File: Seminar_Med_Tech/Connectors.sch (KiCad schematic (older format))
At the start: 21 parts

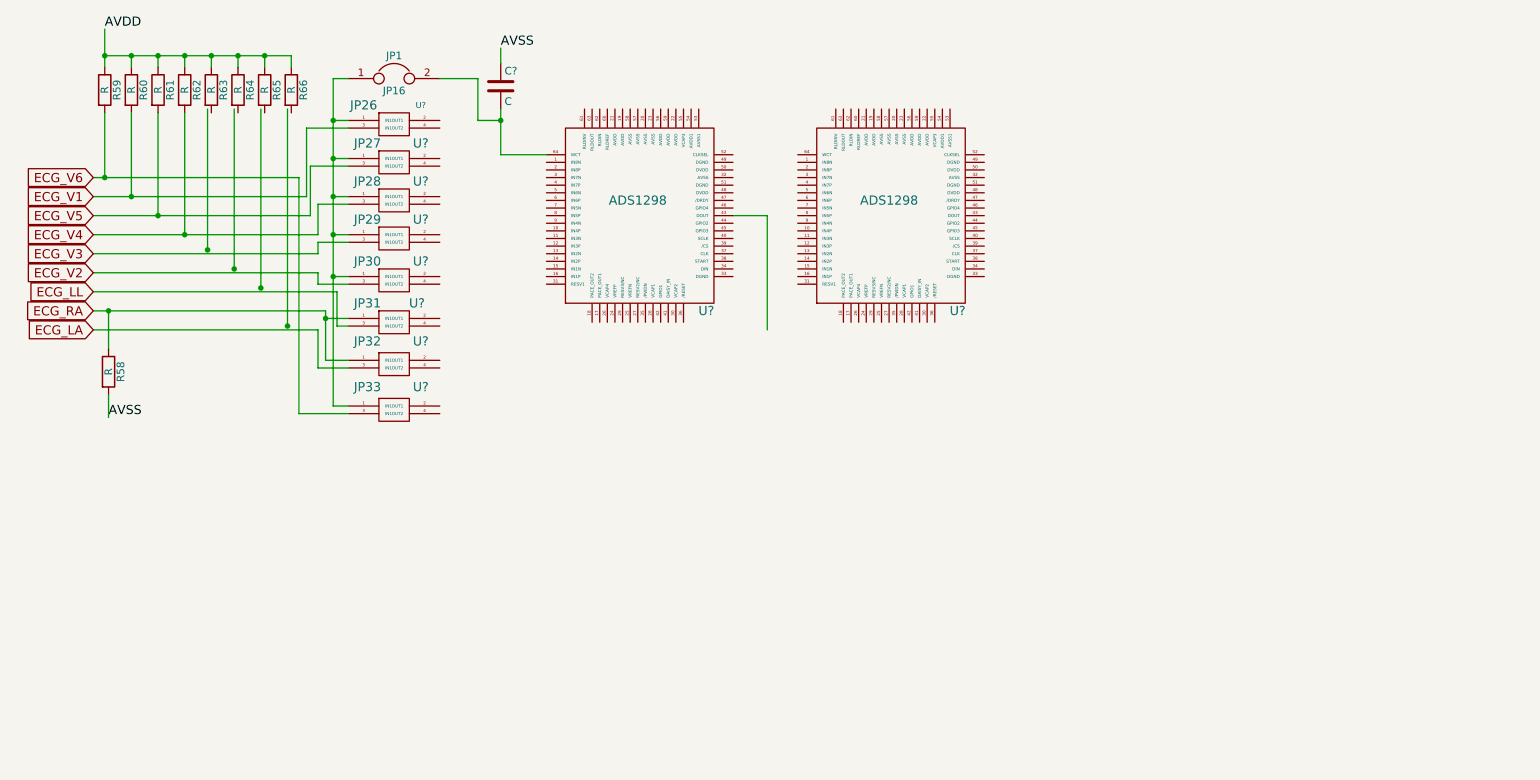
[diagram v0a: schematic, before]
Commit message: Updated Dokumentation and connectors
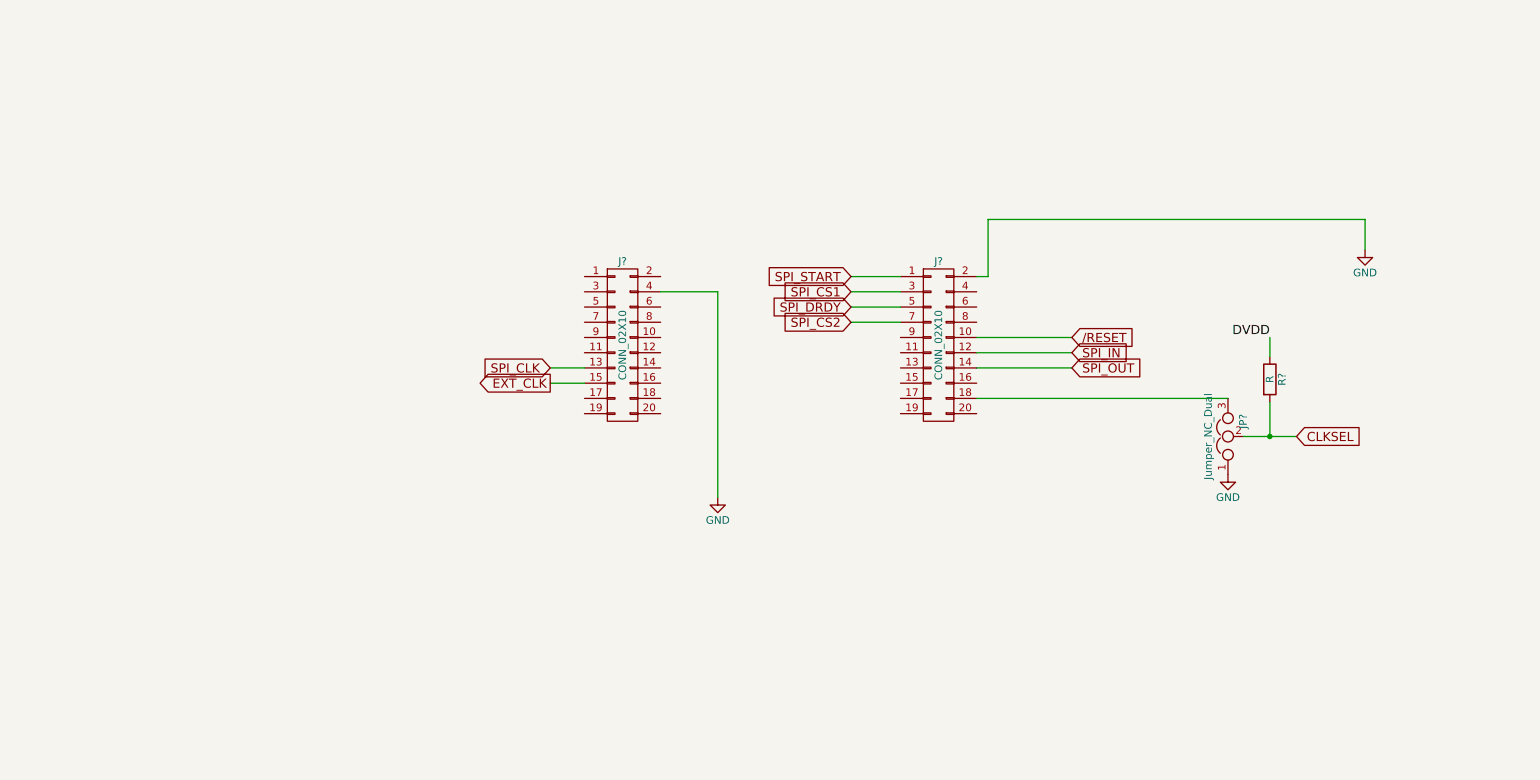
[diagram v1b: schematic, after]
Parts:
- removed C?: C, symbol C
- removed JP1: JP16, symbol Jumper
- removed R58, R59, R60, R61, R62, R63, R64, R65, R66: R, symbol R
- removed U?: JP26, symbol Jumper2x2
- removed U?: JP27, symbol Jumper2x2
- removed U?: JP28, symbol Jumper2x2
- removed U?: JP29, symbol Jumper2x2
- removed U?: JP30, symbol Jumper2x2
- removed U?: JP31, symbol Jumper2x2
- removed U?: JP32, symbol Jumper2x2
- removed U?: JP33, symbol Jumper2x2
- removed U? (x2): ADS1298, symbol ADS1298
- added J? (x2): CONN_02X10, symbol CONN_02X10
- added JP?: Jumper_NC_Dual, symbol Jumper_NC_Dual
- added R?: R, symbol R
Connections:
- net labels added: /RESET, CLKSEL, DVDD, EXT_CLK, GND, SPI_CLK, SPI_CS1, SPI_CS2, SPI_DRDY, SPI_IN, SPI_OUT, SPI_START
- net labels removed: AVDD, AVSS, ECG_LA, ECG_LL, ECG_RA, ECG_V1, ECG_V2, ECG_V3, ECG_V4, ECG_V5, ECG_V6
- wire segments 63 -> 19

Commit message: Updated connectors
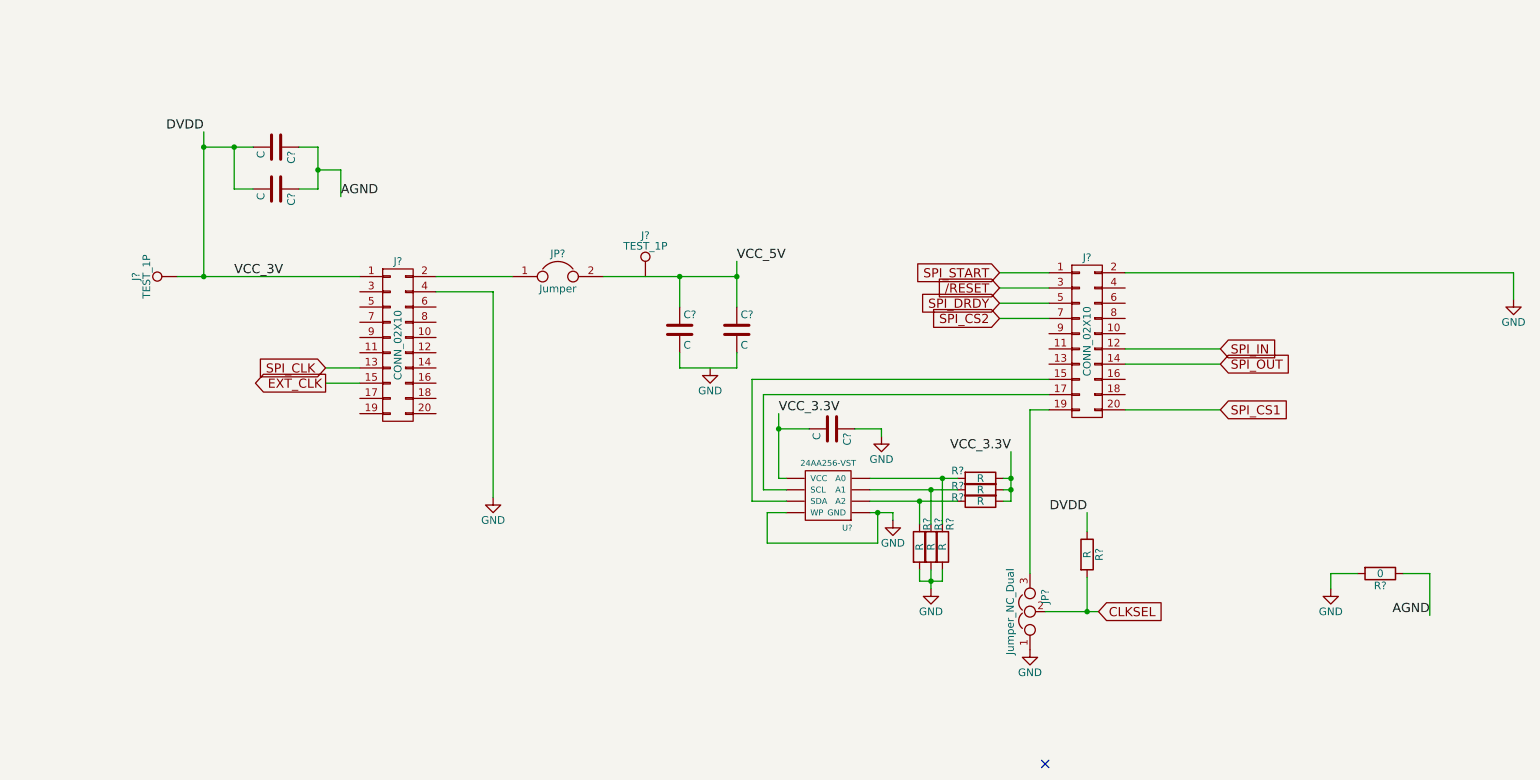
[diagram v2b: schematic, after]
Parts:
- added C? (x5): C, symbol C
- added J? (x2): TEST_1P, symbol TEST_1P
- added JP?: Jumper, symbol Jumper
- added R?: 0, symbol R
- added R? (x6): R, symbol R
- added U?: 24AA256-VST, symbol 24AA256-VST
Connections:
- net /RESET: now also J?.3 (P3); no longer J?.10 (P10)
- net DVDD: now also J?.1 (P1), C?.2, C?.2, J?.1
- net GND: now also C?.1, R?.2, R?.2, R?.2, R?.2, U?.~ (WP)
- net SPI_CS1: now also J?.20 (P20); no longer J?.3 (P3)
- net at J?.2 (P2): now also JP?.1
- net at J?.15 (P15): now also U?.~ (WP)
- net at J?.17 (P17): now also U?.~ (WP)
- net at J?.18 (P18): no longer JP?.3
- net at J?.19 (P19): now also JP?.3
- new net: C?.2, C?.2
- new net: R?.1, R?.2, U?.~ (WP) (x3)
- new net AGND: C?.1, C?.1, R?.1
- new net VCC_3.3V: C?.2, R?.1, R?.1, R?.1, U?.~ (WP)
- new net VCC_5V: C?.1, C?.1, JP?.2
- no-connect marks 0 -> 1
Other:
- moved on the sheet: J?, JP?, R?

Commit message: Updated connectors
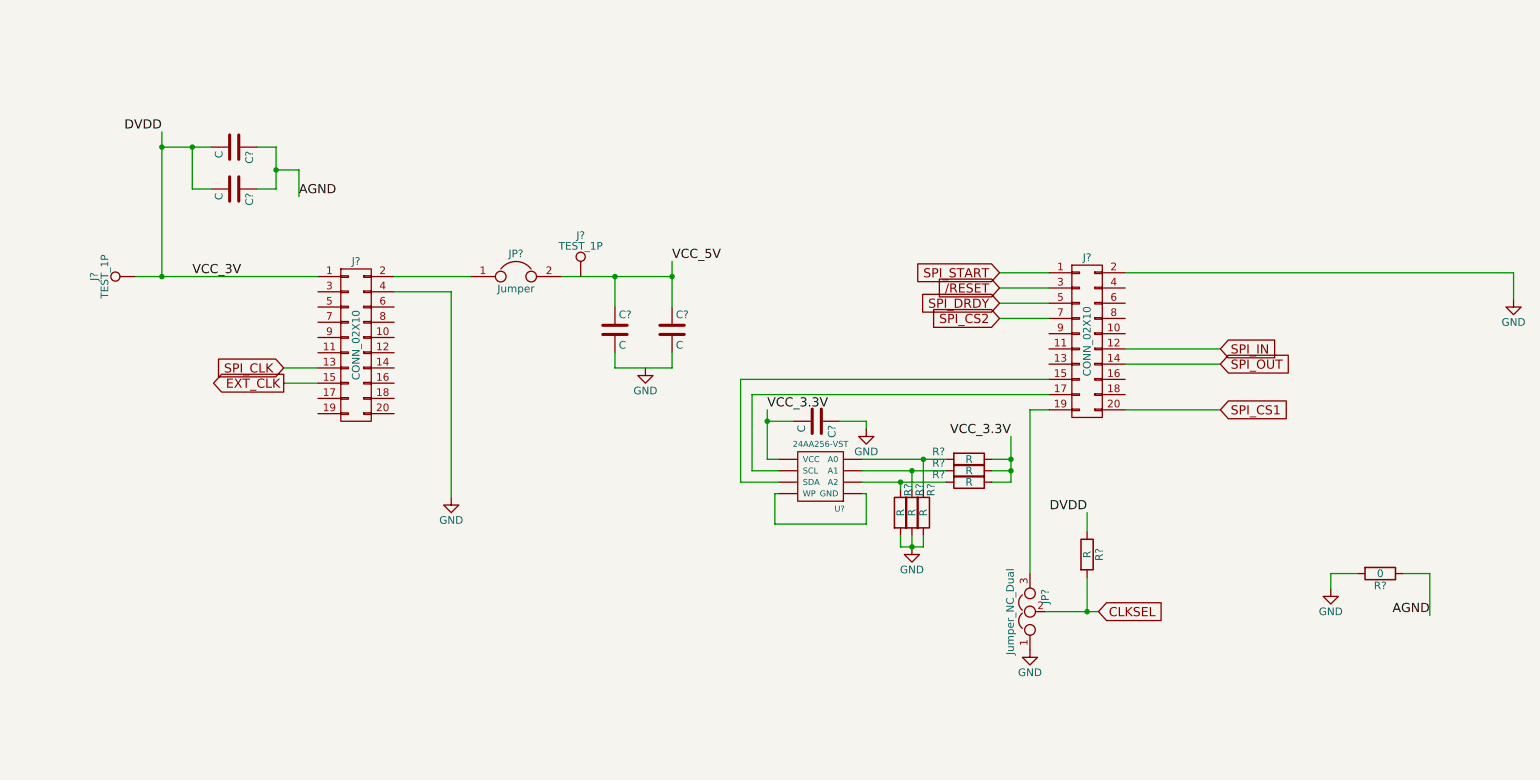
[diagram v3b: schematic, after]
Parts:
- removed C?: C, symbol C
- removed R? (x6): R, symbol R
- removed U?: 24AA256-VST, symbol 24AA256-VST
- added C?: C, symbol C
- added R? (x6): R, symbol R
- added U?: 24AA256-VST, symbol 24AA256-VST
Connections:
- net GND: now also C?.1, R?.2, R?.2, R?.2
- net VCC_3.3V: now also C?.2, R?.1, R?.1, R?.1, U?.~ (WP)
- net at J?.15 (P15): now also U?.~ (WP)
- net at J?.17 (P17): now also U?.~ (WP)
- new net: R?.1, R?.2, U?.~ (WP) (x3)
- no-connect marks 1 -> 0
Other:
- moved on the sheet: C?, J?, JP?

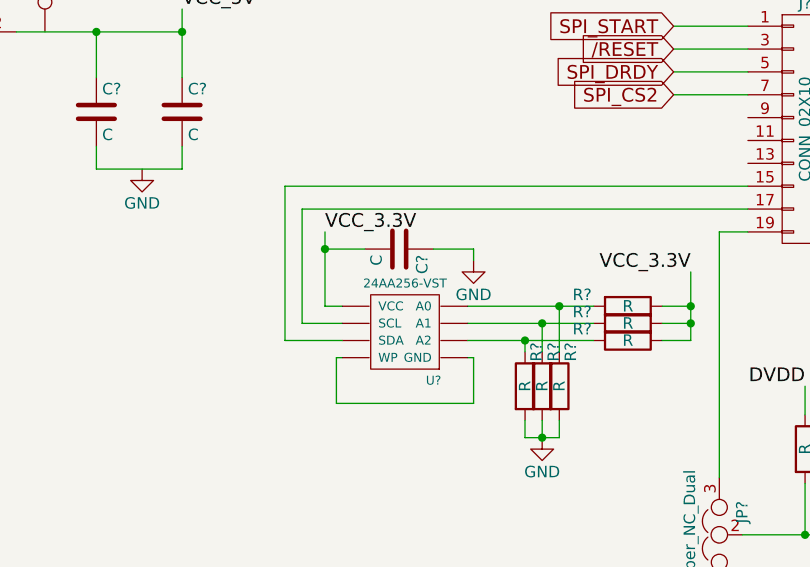
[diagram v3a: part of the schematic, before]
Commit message: Updated connectors
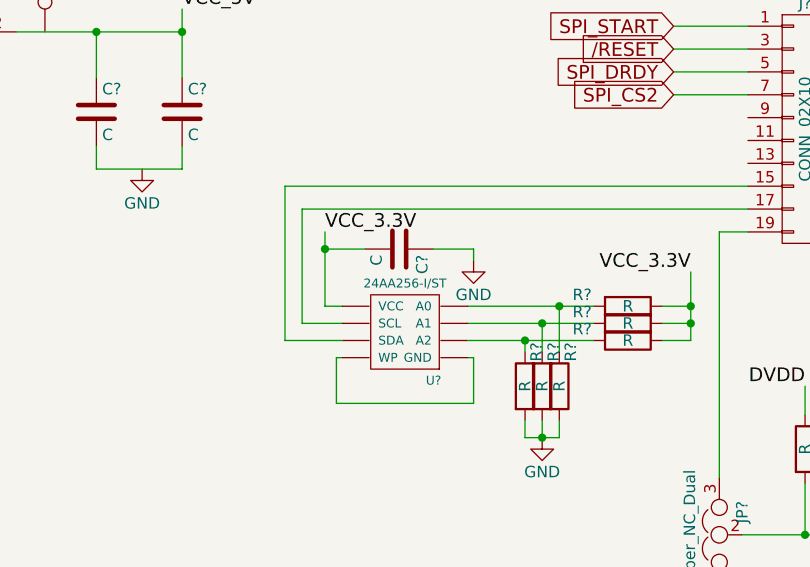
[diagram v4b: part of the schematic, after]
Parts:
- removed U?: 24AA256-VST, symbol 24AA256-VST
- added U?: 24AA256-I/ST, symbol 24AA256-I/ST
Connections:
- net VCC_3.3V: now also U?.~ (WP)
- net at J?.15 (P15): now also U?.~ (WP)
- net at J?.17 (P17): now also U?.~ (WP)
- net at R?.1, R?.2: now also U?.~ (WP) (x3)
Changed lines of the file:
@@
 VCC_5V
-$Comp
-L 24AA256-VST U?
-U 1 1 593E8EFE
-P 5850 4875
-F 0 "U?" H 5975 4675 39  0000 C CNN
-F 1 "24AA256-VST" H 5850 5100 39  0000 C CNN
-F 2 "" H 5850 4875 60  0001 C CNN
-F 3 "" H 5850 4875 60  0001 C CNN
-	1    5850 4875
-	1    0    0    -1
-$EndComp
 $Comp
 L C C?
@@
 Text Label 5500 4425 0    60   ~ 0
 VCC_3.3V
+$Comp
+L 24AA256-I/ST U?
+U 1 1 593E975F
+P 5850 4875
+F 0 "U?" H 5975 4675 39  0000 C CNN
+F 1 "24AA256-I/ST" H 5850 5100 39  0000 C CNN
+F 2 "" H 5850 4875 60  0001 C CNN
+F 3 "" H 5850 4875 60  0001 C CNN
+	1    5850 4875
+	1    0    0    -1
+$EndComp
 $EndSCHEMATC

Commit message: Updated
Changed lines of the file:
@@
 L GND #PWR?
 U 1 1 593AE149
-P 10400 3700
-F 0 "#PWR?" H 10400 3450 50  0001 C CNN
-F 1 "GND" H 10400 3550 50  0000 C CNN
-F 2 "" H 10400 3700 50  0001 C CNN
-F 3 "" H 10400 3700 50  0001 C CNN
-	1    10400 3700
+P 8900 3700
+F 0 "#PWR?" H 8900 3450 50  0001 C CNN
+F 1 "GND" H 8900 3550 50  0000 C CNN
+F 2 "" H 8900 3700 50  0001 C CNN
+F 3 "" H 8900 3700 50  0001 C CNN
+	1    8900 3700
 	1    0    0    -1
 $EndComp
@@
 	3425 3650 3425 5000
 Wire Wire Line
-	7850 3525 10400 3525
-Wire Wire Line
-	10400 3525 10400 3700
+	7850 3525 8900 3525
+Wire Wire Line
+	8900 3525 8900 3700
 Wire Wire Line
 	7850 4425 8475 4425

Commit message: Update
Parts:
- removed C?: C, symbol C
- removed R? (x6): R, symbol R
- removed U?: 24AA256-I/ST, symbol 24AA256-I/ST
- JP21: renamed from JP?; value Jumper_NC_Dual -> Jumper
- gave numbers to parts that had none: 1
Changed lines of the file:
@@
 EXT_CLK
 $Comp
-L Jumper_NC_Dual JP?
+L Jumper_NC_Dual JP21
 U 1 1 593ADF16
 P 7225 5750
-F 0 "JP?" H 7275 5650 50  0000 L CNN
-F 1 "Jumper_NC_Dual" H 7225 5850 50  0000 C BNN
+F 0 "JP21" H 7275 5650 50  0000 L CNN
+F 1 "Jumper" H 7225 5850 50  0000 C BNN
 F 2 "" H 7225 5750 50  0001 C CNN
 F 3 "" H 7225 5750 50  0001 C CNN
@@
 AGND
 $Comp
-L Jumper JP?
+L Jumper JP3
 U 1 1 593E89D7
 P 3850 3550
-F 0 "JP?" H 3850 3700 50  0000 C CNN
+F 0 "JP3" H 3850 3700 50  0000 C CNN
 F 1 "Jumper" H 3850 3470 50  0000 C CNN
 F 2 "" H 3850 3550 50  0001 C CNN
@@
 Text Label 4875 3450 0    60   ~ 0
 VCC_5V
-$Comp
-L C C?
-U 1 1 593E9129
-P 5825 4500
-F 0 "C?" H 5850 4600 50  0000 L CNN
-F 1 "C" H 5850 4400 50  0000 L CNN
-F 2 "" H 5863 4350 50  0001 C CNN
-F 3 "" H 5825 4500 50  0001 C CNN
-	1    5825 4500
-	0    1    1    0
-$EndComp
-$Comp
-L GND #PWR?
-U 1 1 593E9213
-P 6150 4550
-F 0 "#PWR?" H 6150 4300 50  0001 C CNN
-F 1 "GND" H 6150 4400 50  0000 C CNN
-F 2 "" H 6150 4550 50  0001 C CNN
-F 3 "" H 6150 4550 50  0001 C CNN
-	1    6150 4550
-	1    0    0    -1
-$EndComp
-$Comp
-L R R?
-U 1 1 593E92E1
-P 6825 4750
-F 0 "R?" V 6775 4550 50  0000 C CNN
-F 1 "R" V 6825 4750 50  0000 C CNN
-F 2 "" V 6755 4750 50  0001 C CNN
-F 3 "" H 6825 4750 50  0001 C CNN
-	1    6825 4750
-	0    1    1    0
-$EndComp
-$Comp
-L R R?
-U 1 1 593E9373
-P 6825 4825
-F 0 "R?" V 6775 4625 50  0000 C CNN
-F 1 "R" V 6825 4825 50  0000 C CNN
-F 2 "" V 6755 4825 50  0001 C CNN
-F 3 "" H 6825 4825 50  0001 C CNN
-	1    6825 4825
-	0    1    1    0
-$EndComp
-$Comp
-L R R?
-U 1 1 593E946E
-P 6825 4900
-F 0 "R?" V 6775 4700 50  0000 C CNN
-F 1 "R" V 6825 4900 50  0000 C CNN
-F 2 "" V 6755 4900 50  0001 C CNN
-F 3 "" H 6825 4900 50  0001 C CNN
-	1    6825 4900
-	0    1    1    0
-$EndComp
-Text Label 7100 4600 2    60   ~ 0
-VCC_3.3V
-$Comp
-L R R?
-U 1 1 593E9A02
-P 6525 5100
-F 0 "R?" V 6575 5250 50  0000 C CNN
-F 1 "R" V 6525 5100 50  0000 C CNN
-F 2 "" V 6455 5100 50  0001 C CNN
-F 3 "" H 6525 5100 50  0001 C CNN
-	1    6525 5100
-	1    0    0    -1
-$EndComp
-$Comp
-L R R?
-U 1 1 593E9A4D
-P 6450 5100
-F 0 "R?" V 6500 5250 50  0000 C CNN
-F 1 "R" V 6450 5100 50  0000 C CNN
-F 2 "" V 6380 5100 50  0001 C CNN
-F 3 "" H 6450 5100 50  0001 C CNN
-	1    6450 5100
-	1    0    0    -1
-$EndComp
-$Comp
-L R R?
-U 1 1 593E9A8E
-P 6375 5100
-F 0 "R?" V 6425 5250 50  0000 C CNN
-F 1 "R" V 6375 5100 50  0000 C CNN
-F 2 "" V 6305 5100 50  0001 C CNN
-F 3 "" H 6375 5100 50  0001 C CNN
-	1    6375 5100
-	1    0    0    -1
-$EndComp
 Wire Wire Line
 	2550 4150 2325 4150
@@
 	4875 4150 4875 4050
 Connection ~ 4875 3550
-Wire Wire Line
-	5575 4825 5400 4825
-Wire Wire Line
-	5400 4825 5400 4325
-Wire Wire Line
-	5400 4325 7350 4325
-Wire Wire Line
-	7350 4225 5325 4225
-Wire Wire Line
-	5325 4225 5325 4900
-Wire Wire Line
-	5325 4900 5575 4900
-Wire Wire Line
-	6125 4975 6150 4975
-Wire Wire Line
-	6150 4975 6150 5175
-Wire Wire Line
-	6150 5175 5550 5175
-Wire Wire Line
-	5550 5175 5550 4975
-Wire Wire Line
-	5550 4975 5575 4975
-Wire Wire Line
-	5500 4425 5500 4500
-Wire Wire Line
-	5500 4500 5500 4750
-Wire Wire Line
-	5500 4750 5575 4750
-Wire Wire Line
-	5675 4500 5500 4500
-Connection ~ 5500 4500
-Wire Wire Line
-	5975 4500 6150 4500
-Wire Wire Line
-	6150 4500 6150 4550
-Wire Wire Line
-	6675 4750 6525 4750
-Wire Wire Line
-	6525 4750 6125 4750
-Wire Wire Line
-	6125 4825 6450 4825
-Wire Wire Line
-	6450 4825 6675 4825
-Wire Wire Line
-	6675 4900 6375 4900
-Wire Wire Line
-	6375 4900 6125 4900
-Wire Wire Line
-	6975 4750 7100 4750
-Wire Wire Line
-	7100 4825 6975 4825
-Wire Wire Line
-	7100 4900 6975 4900
-Wire Wire Line
-	7100 4600 7100 4750
-Wire Wire Line
-	7100 4750 7100 4825
-Wire Wire Line
-	7100 4825 7100 4900
-Connection ~ 7100 4825
-Connection ~ 7100 4750
-Wire Wire Line
-	6525 4750 6525 4950
-Connection ~ 6525 4750
-Wire Wire Line
-	6450 4950 6450 4825
-Connection ~ 6450 4825
-Wire Wire Line
-	6375 4900 6375 4950
-Connection ~ 6375 4900
-Wire Wire Line
-	6375 5250 6375 5325
-Wire Wire Line
-	6375 5325 6450 5325
-Wire Wire Line
-	6450 5325 6525 5325
-Wire Wire Line
-	6525 5325 6525 5250
-Wire Wire Line
-	6450 5250 6450 5325
-Connection ~ 6450 5325
-$Comp
-L GND #PWR?
-U 1 1 593E9DBC
-P 6450 5325
-F 0 "#PWR?" H 6450 5075 50  0001 C CNN
-F 1 "GND" H 6450 5175 50  0000 C CNN
-F 2 "" H 6450 5325 50  0001 C CNN
-F 3 "" H 6450 5325 50  0001 C CNN
-	1    6450 5325
-	1    0    0    -1
-$EndComp
-Text Label 5500 4425 0    60   ~ 0
-VCC_3.3V
-$Comp
-L 24AA256-I/ST U?
-U 1 1 593E975F
-P 5850 4875
-F 0 "U?" H 5975 4675 39  0000 C CNN
-F 1 "24AA256-I/ST" H 5850 5100 39  0000 C CNN
-F 2 "" H 5850 4875 60  0001 C CNN
-F 3 "" H 5850 4875 60  0001 C CNN
-	1    5850 4875
-	1    0    0    -1
-$EndComp
 $EndSCHEMATC

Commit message: Update
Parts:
- C68, C71: renamed from C?; value C -> 100uF
- C69, C70: renamed from C?; value C -> 0.1uF
- J?: value TEST_1P -> TP10
- J?: value TEST_1P -> TP7
- R67: renamed from R?; value R -> 10K
- gave numbers to parts that had none: 1
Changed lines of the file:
@@
 CLKSEL
 $Comp
-L R R?
+L R R67
 U 1 1 593ADFF6
 P 7600 5375
-F 0 "R?" V 7680 5375 50  0000 C CNN
-F 1 "R" V 7600 5375 50  0000 C CNN
+F 0 "R67" V 7680 5375 50  0000 C CNN
+F 1 "10K" V 7600 5375 50  0000 C CNN
 F 2 "" V 7530 5375 50  0001 C CNN
 F 3 "" H 7600 5375 50  0001 C CNN
@@
 $EndComp
 $Comp
-L R R?
+L R R74
 U 1 1 593E72CF
 P 9525 5500
-F 0 "R?" V 9605 5500 50  0000 C CNN
+F 0 "R74" V 9605 5500 50  0000 C CNN
 F 1 "0" V 9525 5500 50  0000 C CNN
 F 2 "" V 9455 5500 50  0001 C CNN
@@
 P 1350 3550
 F 0 "J?" H 1350 3820 50  0000 C CNN
-F 1 "TEST_1P" H 1350 3750 50  0000 C CNN
+F 1 "TP10" H 1350 3750 50  0000 C CNN
 F 2 "" H 1550 3550 50  0001 C CNN
 F 3 "" H 1550 3550 50  0001 C CNN
@@
 DVDD
 $Comp
-L C C?
+L C C71
 U 1 1 593E8011
 P 2000 2700
-F 0 "C?" H 2025 2800 50  0000 L CNN
-F 1 "C" H 2025 2600 50  0000 L CNN
+F 0 "C71" H 2025 2800 50  0000 L CNN
+F 1 "100uF" H 2025 2600 50  0000 L CNN
 F 2 "" H 2038 2550 50  0001 C CNN
 F 3 "" H 2000 2700 50  0001 C CNN
@@
 $EndComp
 $Comp
-L C C?
+L C C70
 U 1 1 593E8072
 P 2000 2975
-F 0 "C?" H 2025 3075 50  0000 L CNN
-F 1 "C" H 2025 2875 50  0000 L CNN
+F 0 "C70" H 2025 3075 50  0000 L CNN
+F 1 "0.1uF" H 2025 2875 50  0000 L CNN
 F 2 "" H 2038 2825 50  0001 C CNN
 F 3 "" H 2000 2975 50  0001 C CNN
@@
 P 4275 3550
 F 0 "J?" H 4275 3820 50  0000 C CNN
-F 1 "TEST_1P" H 4275 3750 50  0000 C CNN
+F 1 "TP7" H 4275 3750 50  0000 C CNN
 F 2 "" H 4475 3550 50  0001 C CNN
 F 3 "" H 4475 3550 50  0001 C CNN
@@
 $EndComp
 $Comp
-L C C?
+L C C69
 U 1 1 593E9092
 P 4500 3900
-F 0 "C?" H 4525 4000 50  0000 L CNN
-F 1 "C" H 4525 3800 50  0000 L CNN
+F 0 "C69" H 4525 4000 50  0000 L CNN
+F 1 "0.1uF" H 4525 3800 50  0000 L CNN
 F 2 "" H 4538 3750 50  0001 C CNN
 F 3 "" H 4500 3900 50  0001 C CNN
@@
 $EndComp
 $Comp
-L C C?
+L C C68
 U 1 1 593E90E8
 P 4875 3900
-F 0 "C?" H 4900 4000 50  0000 L CNN
-F 1 "C" H 4900 3800 50  0000 L CNN
+F 0 "C68" H 4900 4000 50  0000 L CNN
+F 1 "100uF" H 4900 3800 50  0000 L CNN
 F 2 "" H 4913 3750 50  0001 C CNN
 F 3 "" H 4875 3900 50  0001 C CNN
